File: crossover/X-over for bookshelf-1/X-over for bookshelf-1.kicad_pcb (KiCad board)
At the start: 2 copper layers, 121.8 x 137.2 mm, 14 parts, among them J1 Input, J2 Output

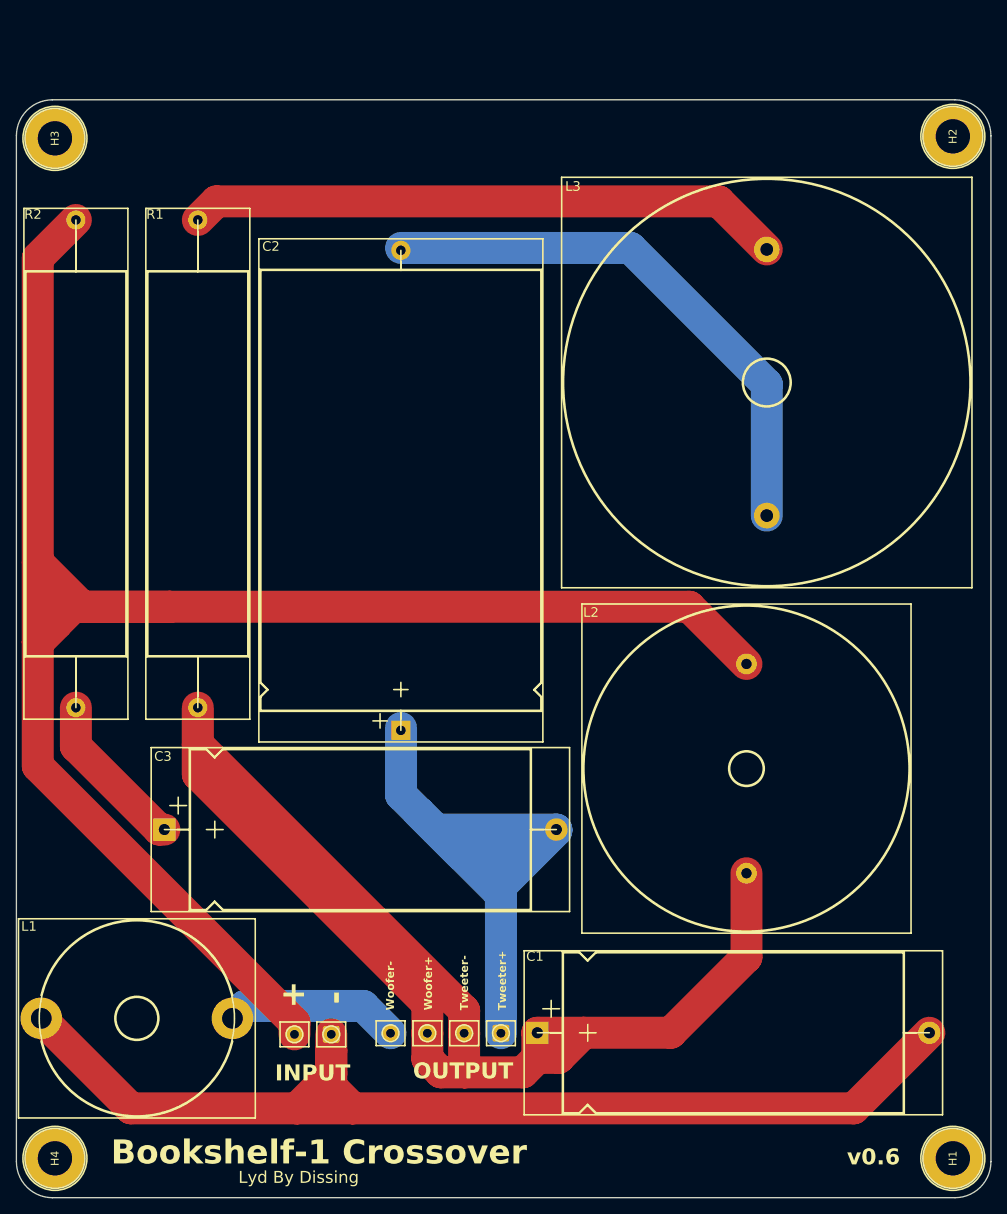
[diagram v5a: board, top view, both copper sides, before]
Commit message: making the overall PCB a lot smaller, so it fits through the driver hole
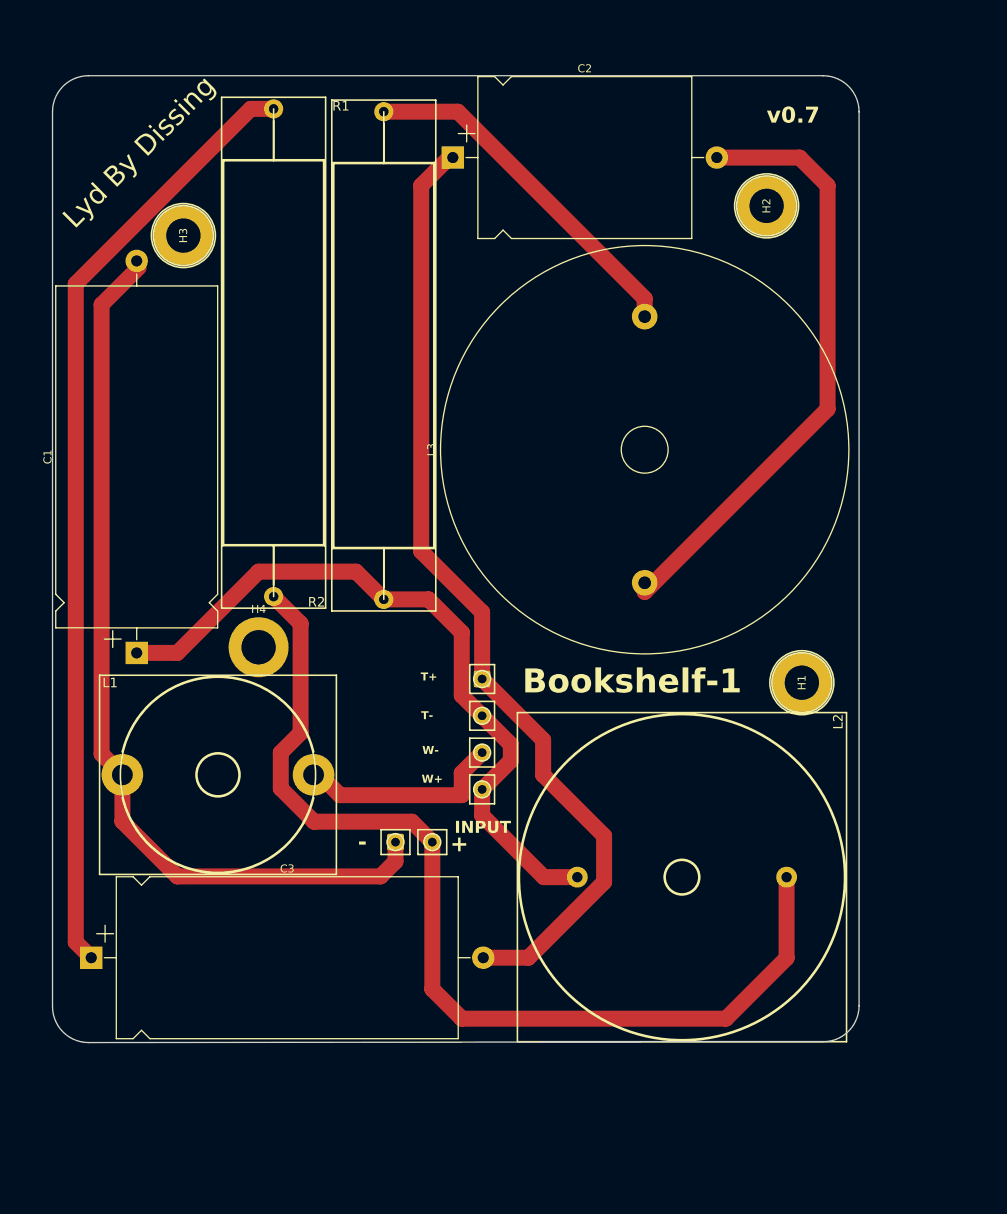
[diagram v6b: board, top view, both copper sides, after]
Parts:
- C2: footprint Capacitor_THT:CP_Axial_L55.0mm_D35.0mm_P60.00mm_Horizontal -> Capacitor_THT:CP_Axial_L26.5mm_D20.0mm_P33.00mm_Horizontal
- moved C2 71.9 mm to (97.9, 49.8), turned to 0 degrees
- moved C1 69.0 mm to (58.4, 111.8), turned to 90 degrees
- moved H4 68.8 mm to (73.7, 111.0), turned to 0 degrees
- moved H1 62.4 mm to (141.6, 115.5)
- moved R2 53.2 mm to (75.5, 104.7), turned to 90 degrees
- moved J2 44.3 mm to (101.6, 115.0), turned to -90 degrees
- moved L1 32.1 mm to (56.6, 127.0)
- moved L2 27.1 mm to (139.7, 139.8), turned to 180 degrees
- moved R1 26.9 mm to (89.3, 44.1)
- moved J1 25.3 mm to (90.8, 135.4), turned to 0 degrees
- moved H2 24.8 mm to (137.2, 55.9)
- moved H3 20.1 mm to (64.3, 59.6)
- moved C3 18.4 mm to (52.7, 149.9)
- moved L3 17.4 mm to (121.9, 103.0)
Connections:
- J2 pad 3: Net-(J2-Pin_2) -> Net-(J2-Pin_3)
- J2 pad 4: Net-(J2-Pin_4) -> Net-(J2-Pin_2)
- L1 pad 2: Net-(J2-Pin_4) -> Net-(J2-Pin_3)
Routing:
- net Net-(J1-Pin_2): track 235.3 -> 125.6 mm
- net Net-(C3-Pad1): track 20.2 -> 118.8 mm
- net Net-(J2-Pin_2): track 176.6 -> 90.0 mm
- net Net-(J2-Pin_1): track 86.1 -> 121.0 mm
- net Net-(L3-Pad2): track 74.6 -> 44.6 mm
- net Net-(J1-Pin_1): track 139.0 -> 112.4 mm
- net Net-(J2-Pin_3): track 0.00 -> 25.9 mm
- net Net-(J2-Pin_4): track 21.8 -> 0.00 mm
- net Net-(C2-Pad2): track 69.2 -> 76.7 mm
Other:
- board size 121.8 x 137.2 mm -> 100.8 x 120.9 mm
- board text added: "Bookshelf-1"
- board text added: "T+"
- board text added: "T-"
- board text added: "W+"
- board text added: "W-"
- board text added: "v0.7"
- board text removed: "Bookshelf-1 Crossover"
- board text removed: "OUTPUT"
- board text removed: "Tweeter+"
- board text removed: "Tweeter-"
- board text removed: "Woofer+"
- board text removed: "Woofer-"
- board text removed: "v0.6"
